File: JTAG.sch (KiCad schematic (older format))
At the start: 27 parts, among them CN5 CONN_RCPT_USB2.0_MINI_B_SMD_R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, U15 FT2232HL-REEL, U9 LDL212D33R, X2 ABM3B-12.000MHZ

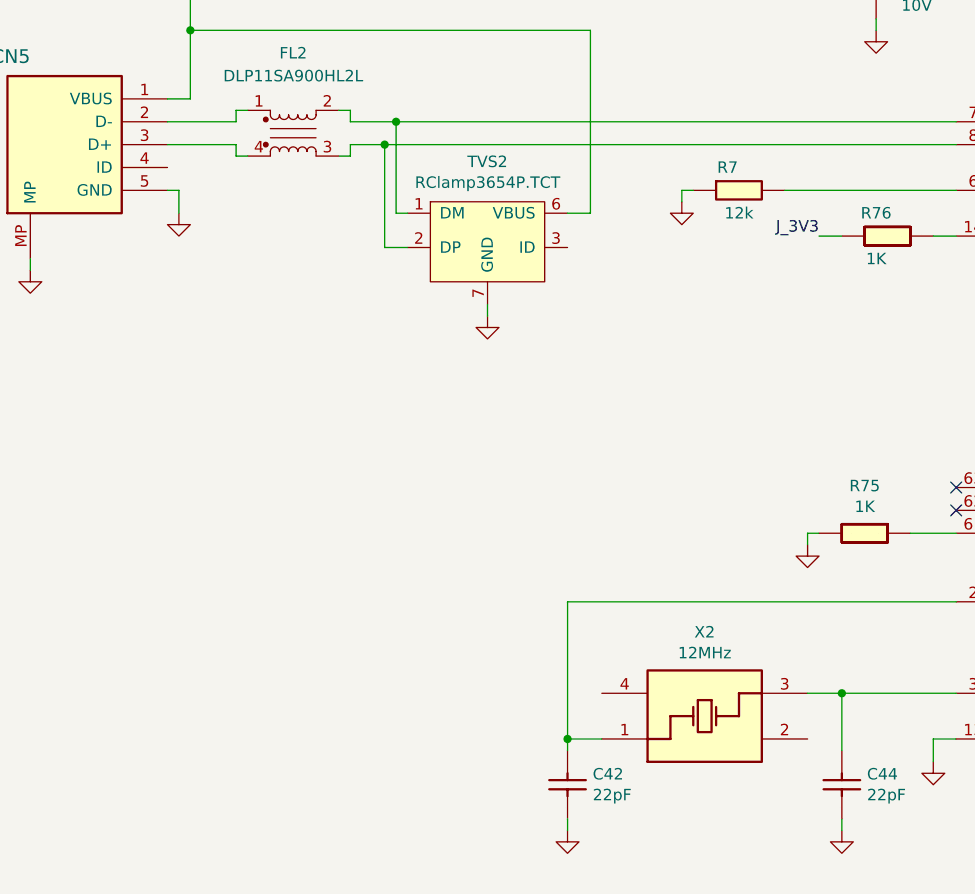
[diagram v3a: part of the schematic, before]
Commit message: Split the design into two boards, main controller board and a power supply board.
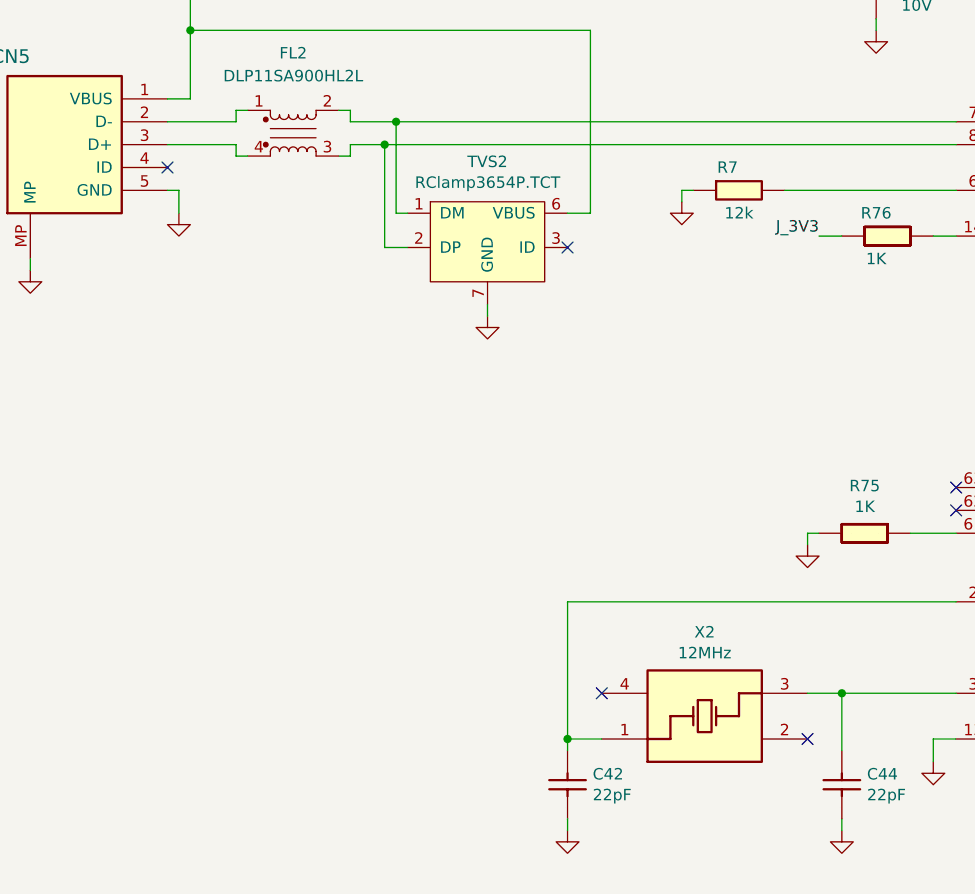
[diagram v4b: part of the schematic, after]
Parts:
- C40, C41, C42, C44, C46, C48, C49, C50, C51, C52, C53, C54, C55: footprint (none) -> Capacitor_SMD:C_0603_1608Metric
- FB2, FB3: footprint (none) -> Inductor_SMD:L_0603_1608Metric
- R75, R76: footprint (none) -> Resistor_SMD:R_0603_1608Metric
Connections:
- no-connect marks 30 -> 34
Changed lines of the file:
@@
 F 0 "FB2" H 3750 1207 50  0000 C CNN
 F 1 "Chip_Ferrite,_600R,_0603,_750mA" H 3750 1208 50  0001 C CNN
-F 2 "" H 3450 900 50  0001 C CNN
+F 2 "Inductor_SMD:L_0603_1608Metric" H 3450 900 50  0001 C CNN
 F 3 "" H 3450 900 50  0001 C CNN
 F 4 "600R" H 3750 1116 50  0000 C CNN "Val"
@@
 F 0 "C40" V 1204 2160 50  0000 L CNN
 F 1 "100nF_0603_Ceramic_Capacitor,_10%,_X7R,_25V" H 1200 2150 50  0001 C CNN
-F 2 "" H 1200 2150 50  0001 C CNN
+F 2 "Capacitor_SMD:C_0603_1608Metric" H 1200 2150 50  0001 C CNN
 F 3 "" H 1200 2150 50  0001 C CNN
 F 4 "100nF" V 1295 2160 50  0000 L CNN "Val"
@@
 F 0 "C41" V 2854 2160 50  0000 L CNN
 F 1 "100nF_0603_Ceramic_Capacitor,_10%,_X7R,_25V" H 2850 2150 50  0001 C CNN
-F 2 "" H 2850 2150 50  0001 C CNN
+F 2 "Capacitor_SMD:C_0603_1608Metric" H 2850 2150 50  0001 C CNN
 F 3 "" H 2850 2150 50  0001 C CNN
 F 4 "100nF" V 2945 2160 50  0000 L CNN "Val"
@@
 F 0 "FB3" H 3750 1757 50  0000 C CNN
 F 1 "Chip_Ferrite,_600R,_0603,_750mA" H 3750 1758 50  0001 C CNN
-F 2 "" H 3450 1450 50  0001 C CNN
+F 2 "Inductor_SMD:L_0603_1608Metric" H 3450 1450 50  0001 C CNN
 F 3 "" H 3450 1450 50  0001 C CNN
 F 4 "600R" H 3750 1666 50  0000 C CNN "Val"
@@
 F 0 "R76" H 4500 3700 50  0000 C CNN
 F 1 "1K_0603_Chip_Resistor,_1%,_0.1W" H 4450 3700 50  0001 C CNN
-F 2 "" H 4450 3700 60  0001 C CNN
+F 2 "Resistor_SMD:R_0603_1608Metric" H 4450 3700 60  0001 C CNN
 F 3 "" H 4450 3700 60  0001 C CNN
 F 4 "1K" H 4500 3500 50  0000 C CNN "Val"
@@
 F 0 "C46" V 4904 1110 50  0000 L CNN
 F 1 "100nF_0603_Ceramic_Capacitor,_10%,_X7R,_25V" H 4900 1100 50  0001 C CNN
-F 2 "" H 4900 1100 50  0001 C CNN
+F 2 "Capacitor_SMD:C_0603_1608Metric" H 4900 1100 50  0001 C CNN
 F 3 "" H 4900 1100 50  0001 C CNN
 F 4 "100nF" V 4995 1110 50  0000 L CNN "Val"
@@
 F 0 "C48" V 6404 1060 50  0000 L CNN
 F 1 "100nF_0603_Ceramic_Capacitor,_10%,_X7R,_25V" H 6400 1050 50  0001 C CNN
-F 2 "" H 6400 1050 50  0001 C CNN
+F 2 "Capacitor_SMD:C_0603_1608Metric" H 6400 1050 50  0001 C CNN
 F 3 "" H 6400 1050 50  0001 C CNN
 F 4 "100nF" V 6495 1060 50  0000 L CNN "Val"
@@
 F 0 "C49" V 7054 960 50  0000 L CNN
 F 1 "100nF_0603_Ceramic_Capacitor,_10%,_X7R,_25V" H 7050 950 50  0001 C CNN
-F 2 "" H 7050 950 50  0001 C CNN
+F 2 "Capacitor_SMD:C_0603_1608Metric" H 7050 950 50  0001 C CNN
 F 3 "" H 7050 950 50  0001 C CNN
 F 4 "100nF" V 7145 960 50  0000 L CNN "Val"
@@
 F 0 "C50" V 7554 960 50  0000 L CNN
 F 1 "100nF_0603_Ceramic_Capacitor,_10%,_X7R,_25V" H 7550 950 50  0001 C CNN
-F 2 "" H 7550 950 50  0001 C CNN
+F 2 "Capacitor_SMD:C_0603_1608Metric" H 7550 950 50  0001 C CNN
 F 3 "" H 7550 950 50  0001 C CNN
 F 4 "100nF" V 7645 960 50  0000 L CNN "Val"
@@
 F 0 "C51" V 8004 960 50  0000 L CNN
 F 1 "100nF_0603_Ceramic_Capacitor,_10%,_X7R,_25V" H 8000 950 50  0001 C CNN
-F 2 "" H 8000 950 50  0001 C CNN
+F 2 "Capacitor_SMD:C_0603_1608Metric" H 8000 950 50  0001 C CNN
 F 3 "" H 8000 950 50  0001 C CNN
 F 4 "100nF" V 8095 960 50  0000 L CNN "Val"
@@
 F 0 "C52" V 8454 960 50  0000 L CNN
 F 1 "100nF_0603_Ceramic_Capacitor,_10%,_X7R,_25V" H 8450 950 50  0001 C CNN
-F 2 "" H 8450 950 50  0001 C CNN
+F 2 "Capacitor_SMD:C_0603_1608Metric" H 8450 950 50  0001 C CNN
 F 3 "" H 8450 950 50  0001 C CNN
 F 4 "100nF" V 8545 960 50  0000 L CNN "Val"
@@
 F 0 "C53" V 8954 960 50  0000 L CNN
 F 1 "100nF_0603_Ceramic_Capacitor,_10%,_X7R,_25V" H 8950 950 50  0001 C CNN
-F 2 "" H 8950 950 50  0001 C CNN
+F 2 "Capacitor_SMD:C_0603_1608Metric" H 8950 950 50  0001 C CNN
 F 3 "" H 8950 950 50  0001 C CNN
 F 4 "100nF" V 9045 960 50  0000 L CNN "Val"
@@
 F 0 "C54" V 9404 960 50  0000 L CNN
 F 1 "100nF_0603_Ceramic_Capacitor,_10%,_X7R,_25V" H 9400 950 50  0001 C CNN
-F 2 "" H 9400 950 50  0001 C CNN
+F 2 "Capacitor_SMD:C_0603_1608Metric" H 9400 950 50  0001 C CNN
 F 3 "" H 9400 950 50  0001 C CNN
 F 4 "100nF" V 9495 960 50  0000 L CNN "Val"
@@
 F 0 "C55" V 9904 960 50  0000 L CNN
 F 1 "100nF_0603_Ceramic_Capacitor,_10%,_X7R,_25V" H 9900 950 50  0001 C CNN
-F 2 "" H 9900 950 50  0001 C CNN
+F 2 "Capacitor_SMD:C_0603_1608Metric" H 9900 950 50  0001 C CNN
 F 3 "" H 9900 950 50  0001 C CNN
 F 4 "100nF" V 9995 960 50  0000 L CNN "Val"
@@
 F 0 "C42" V 3254 6160 50  0000 L CNN
 F 1 "22pF_0603_Ceramic_Capacitor,_5%,_NP0,_50V" H 3250 6150 50  0001 C CNN
-F 2 "" H 3250 6150 50  0001 C CNN
+F 2 "Capacitor_SMD:C_0603_1608Metric" H 3250 6150 50  0001 C CNN
 F 3 "" H 3250 6150 50  0001 C CNN
 F 4 "22pF" V 3345 6160 50  0000 L CNN "Val"
@@
 F 0 "C44" V 4454 6160 50  0000 L CNN
 F 1 "22pF_0603_Ceramic_Capacitor,_5%,_NP0,_50V" H 4450 6150 50  0001 C CNN
-F 2 "" H 4450 6150 50  0001 C CNN
+F 2 "Capacitor_SMD:C_0603_1608Metric" H 4450 6150 50  0001 C CNN
 F 3 "" H 4450 6150 50  0001 C CNN
 F 4 "22pF" V 4545 6160 50  0000 L CNN "Val"
@@
 F 0 "R75" H 4450 5107 50  0000 C CNN
 F 1 "1K_0603_Chip_Resistor,_1%,_0.1W" H 4350 5000 50  0001 C CNN
-F 2 "" H 4350 5000 60  0001 C CNN
+F 2 "Resistor_SMD:R_0603_1608Metric" H 4350 5000 60  0001 C CNN
 F 3 "" H 4350 5000 60  0001 C CNN
 F 4 "1K" H 4450 5016 50  0000 C CNN "Val"
@@
 Wire Wire Line
 	8000 2600 7250 2600
+NoConn ~ 1400 3500
+NoConn ~ 3150 3850
+NoConn ~ 3300 5800
+NoConn ~ 4200 6000
 $EndSCHEMATC

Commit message: Stuff
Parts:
- FL2: symbol F_inductors:DLP11SA900HL2L -> OpenVent-rescue:DLP11SA900HL2L-F_inductors
- TVS2: symbol F_Misc:RClamp3654P.TCT -> OpenVent-rescue:RClamp3654P.TCT-F_Misc
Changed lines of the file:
@@
 $EndComp
 $Comp
-L F_Misc:RClamp3654P.TCT TVS2
+L OpenVent-rescue:RClamp3654P.TCT-F_Misc TVS2
 U 1 1 5FB67D83
 P 2800 4000
@@
 $EndComp
 $Comp
-L F_inductors:DLP11SA900HL2L FL2
+L OpenVent-rescue:DLP11SA900HL2L-F_inductors FL2
 U 1 1 5FB69009
 P 1950 3350

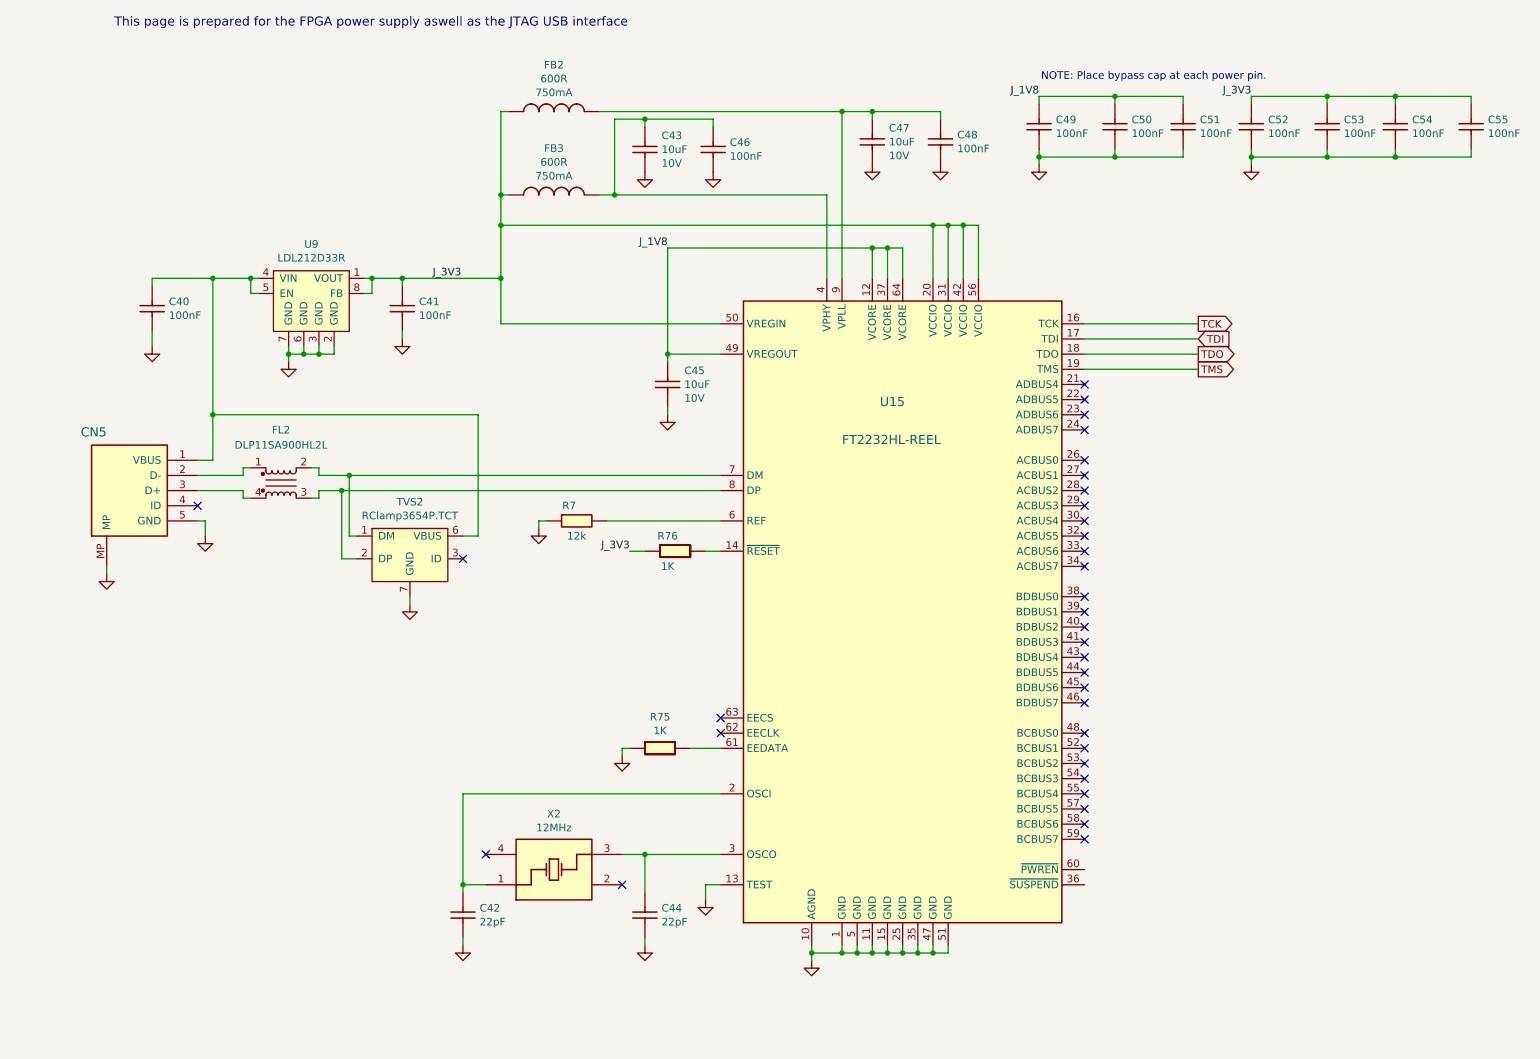
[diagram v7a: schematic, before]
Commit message: Went through the whole circuit and made a note of what needs changing
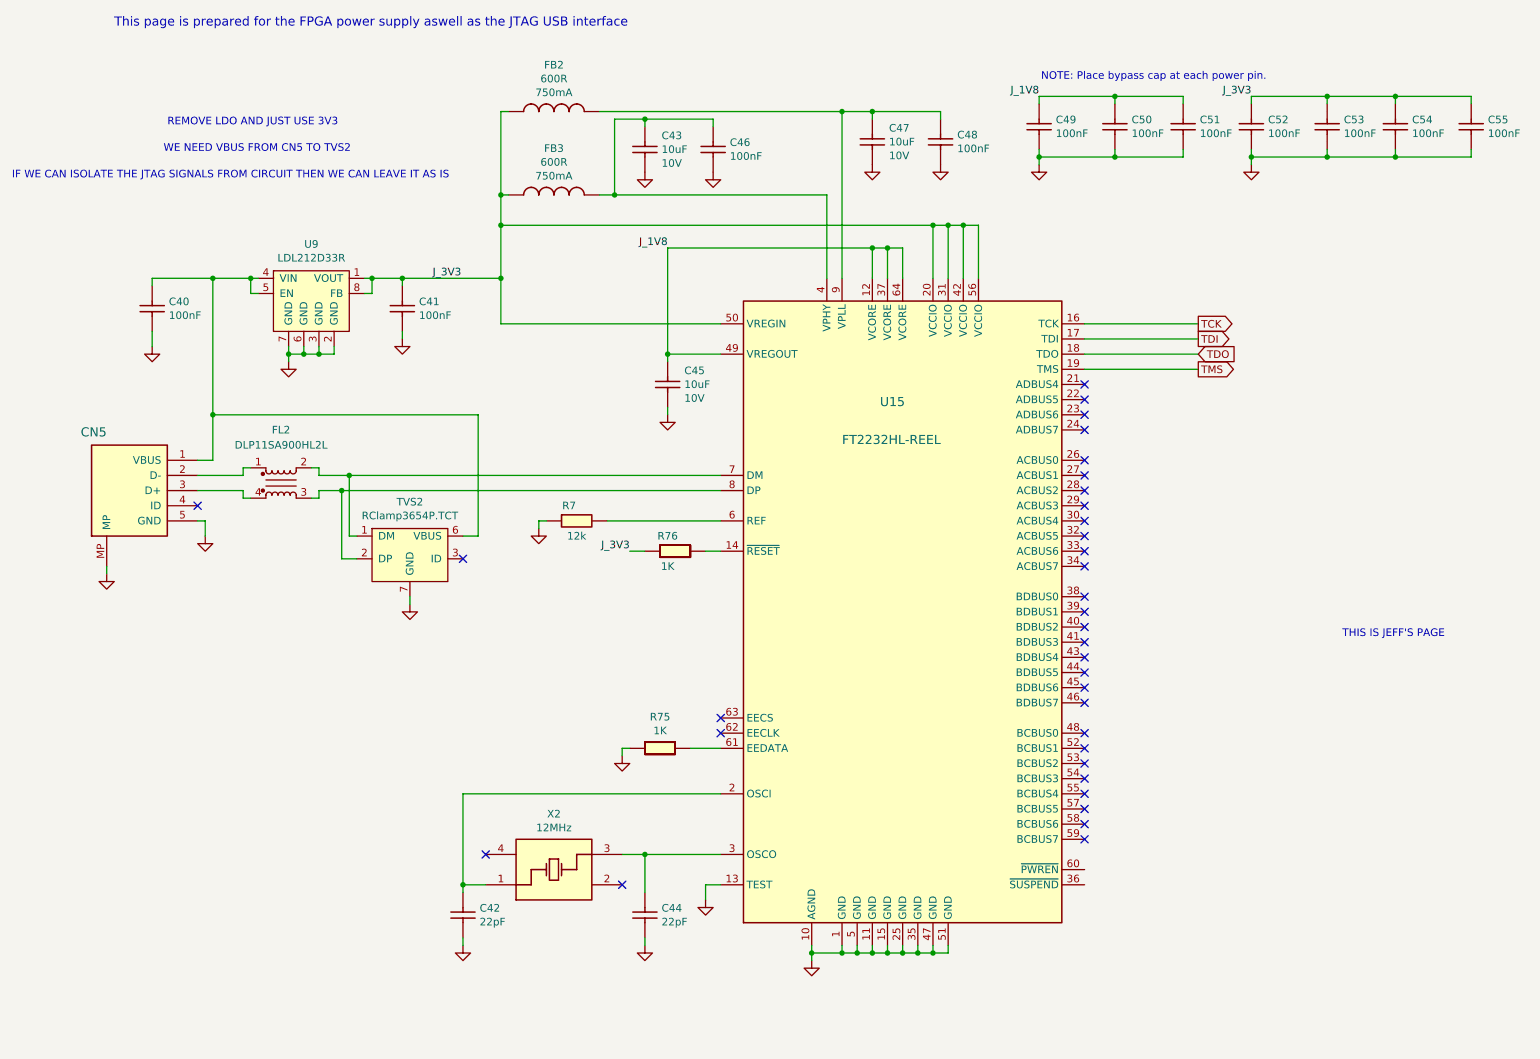
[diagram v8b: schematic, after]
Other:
- note added: "IF WE CAN ISOLATE THE JTAG SIGNALS FROM CIRCUIT THEN WE CAN LEAVE IT AS IS"
- note added: "REMOVE LDO AND JUST USE 3V3\n"
- note added: "THIS IS JEFF'S PAGE\n"
- note added: "WE NEED VBUS FROM CN5 TO TVS2"
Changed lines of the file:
@@
 Text GLabel 8000 2300 2    50   Output ~ 0
 TCK
-Text GLabel 8000 2400 2    50   Input ~ 0
+Text GLabel 8000 2400 2    50   Output ~ 0
 TDI
-Text GLabel 8000 2500 2    50   Output ~ 0
+Text GLabel 8000 2500 2    50   Input ~ 0
 TDO
 Text GLabel 8000 2600 2    50   Output ~ 0
@@
 NoConn ~ 3300 5800
 NoConn ~ 4200 6000
+Text Notes 1175 1175 0    50   ~ 0
+WE NEED VBUS FROM CN5 TO TVS2
+Text Notes 1200 1000 0    50   ~ 0
+REMOVE LDO AND JUST USE 3V3\n
+Text Notes 175  1350 0    50   ~ 0
+IF WE CAN ISOLATE THE JTAG SIGNALS FROM CIRCUIT THEN WE CAN LEAVE IT AS IS
+Text Notes 8950 4375 0    50   ~ 0
+THIS IS JEFF'S PAGE\n
 $EndSCHEMATC
